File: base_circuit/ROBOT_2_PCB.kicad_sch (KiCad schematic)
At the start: 21 parts, among them J1 Conn_01x04, J2 Output_Supply, J3 Conn_01x01_Female, J4 M1,2, J5 M3,4, M1 Conn_01x04_Female, M2 Conn_01x04_Female, M3 Conn_01x04_Female, M4 Conn_01x04_Female, SW1 SW_SPDT, SW2 SW_SPDT

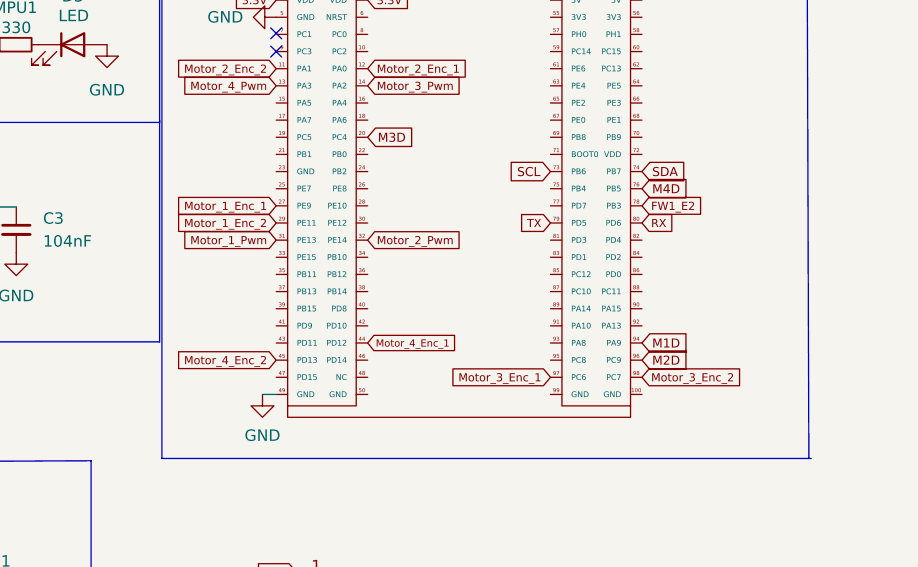
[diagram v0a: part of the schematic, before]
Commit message: Add ioc file od base circuit
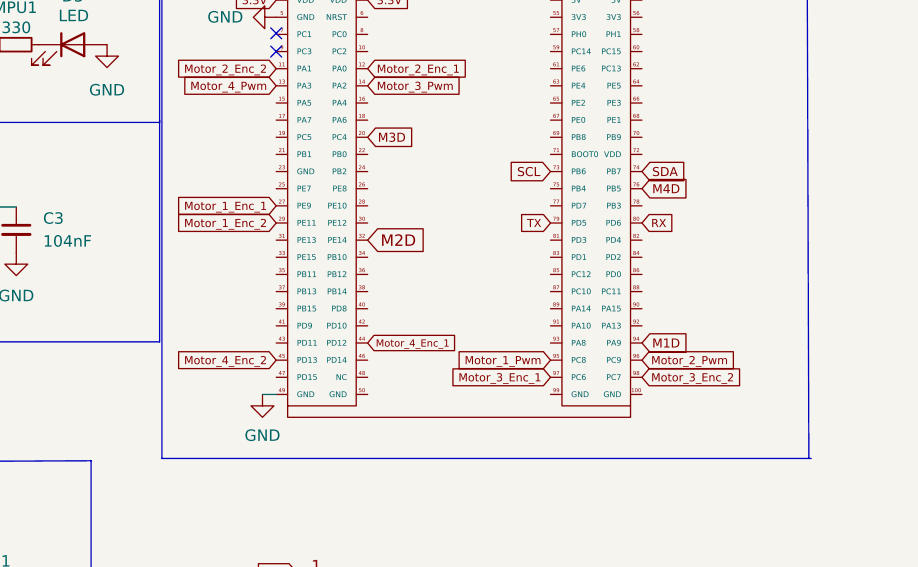
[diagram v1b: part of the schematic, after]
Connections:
- net M2D: now also S1.32 (PE14); no longer S1.96 (PC9)
- net Motor_1_Pwm: now also S1.95 (PC8); no longer S1.31 (PE13)
- net Motor_2_Pwm: now also S1.96 (PC9); no longer S1.32 (PE14)
- net FW1_E2: no longer names the net of S1.78 (PB3)
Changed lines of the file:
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@@
-    )
-  )
-  (global_label "FW1_E2" (shape input) (at 130.048 67.183 0) (fields_autoplaced)
-    (effects (font (size 0.9 0.9)) (justify left))
-    (property "Intersheet References" "${INTERSHEET_REFS}" (id 0) (at 136.7723 67.1268 0)
-      (effects (font (size 0.9 0.9)) (justify left) hide)
     )
   )
@@
     )
   )
+  (global_label "M2D" (shape input) (at 99.568 70.993 0) (fields_autoplaced)
+    (effects (font (size 1.27 1.27)) (justify left))
+    (property "Intersheet References" "${INTERSHEET_REFS}" (id 0) (at 105.9121 70.9136 0)
+      (effects (font (size 1.27 1.27)) (justify left) hide)
+    )
+  )
   (global_label "Motor_2_Enc_2" (shape input) (at 158.496 168.91 180) (fields_autoplaced)
     (effects (font (size 0.9 0.9)) (justify right))
@@
     )
   )
-  (global_label "Motor_1_Pwm" (shape input) (at 89.408 70.993 180) (fields_autoplaced)
-    (effects (font (size 0.9 0.9)) (justify right))
-    (property "Intersheet References" "${INTERSHEET_REFS}" (id 0) (at 78.698 70.9368 0)
+  (global_label "Motor_1_Pwm" (shape input) (at 119.888 84.328 180) (fields_autoplaced)
+    (effects (font (size 0.9 0.9)) (justify right))
+    (property "Intersheet References" "${INTERSHEET_REFS}" (id 0) (at 109.178 84.2718 0)
       (effects (font (size 0.9 0.9)) (justify right) hide)
     )
@@
     (property "Intersheet References" "${INTERSHEET_REFS}" (id 0) (at 107.77 169.8698 0)
       (effects (font (size 0.9 0.9)) (justify right) hide)
-    )
-  )
-  (global_label "M2D" (shape input) (at 130.048 84.328 0) (fields_autoplaced)
-    (effects (font (size 1 1)) (justify left))
-    (property "Intersheet References" "${INTERSHEET_REFS}" (id 0) (at 135.0432 84.2655 0)
-      (effects (font (size 1 1)) (justify left) hide)
     )
   )
@@
     )
   )
-  (global_label "Motor_2_Pwm" (shape input) (at 99.568 70.993 0) (fields_autoplaced)
-    (effects (font (size 0.9 0.9)) (justify left))
-    (property "Intersheet References" "${INTERSHEET_REFS}" (id 0) (at 110.278 70.9368 0)
-      (effects (font (size 0.9 0.9)) (justify left) hide)
-    )
+  (global_label "Motor_2_Pwm" (shape input) (at 130.048 84.328 0) (fields_autoplaced)
+    (effects (font (size 0.9 0.9)) (justify left))
+    (property "Intersheet References" "${INTERSHEET_REFS}" (id 0) (at 140.758 84.2718 0)
+      (effects (font (size 0.9 0.9)) (justify left) hide)
+    )

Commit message: debugging push for singlefile change
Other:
- note added: "laaa****mmmooooo"
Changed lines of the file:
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@@
     (stroke (width 0) (type default) (color 0 0 0 0))
+  )
+  (text "laaa****mmmooooo" (at 22.606 -12.7 0)
+    (effects (font (size 10 10)) (justify left bottom))
   )
   (text "MAIN CONTROLLER BOARD\n" (at 79.248 20.574 0)

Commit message: Final Edit of base circuit
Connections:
- net GND: now also S1.50 (GND)
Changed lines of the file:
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@@
     (pin "4")
+  )
+  (symbol (lib_id "power:GND") (at 99.568 88.138 0) (unit 1)
+    (in_bom yes) (on_board yes) (fields_autoplaced)
+    (property "Reference" "#PWR0112" (id 0) (at 99.568 94.488 0)
+      (effects (font (size 1.27 1.27)) hide)
+    )
+    (property "Value" "GND" (id 1) (at 99.568 92.71 0))
+    (property "Footprint" "" (id 2) (at 99.568 88.138 0)
+      (effects (font (size 1.27 1.27)) hide)
+    )
+    (property "Datasheet" "" (id 3) (at 99.568 88.138 0)
+      (effects (font (size 1.27 1.27)) hide)
+    )
+    (pin "1")
   )
   (symbol (lib_id "Connector_Generic:Conn_01x05") (at 32.004 33.02 0) (unit 1)
@@
       (reference "#PWR0111") (unit 1) (value "GND") (footprint "")
     )
+    (path "/21177c56-f2a5-4c39-9fca-9dfafd9b0072"
+      (reference "#PWR0112") (unit 1) (value "GND") (footprint "")
+    )
     (path "/86c17262-2c7a-4ee7-bb6b-b97ffef60f30"

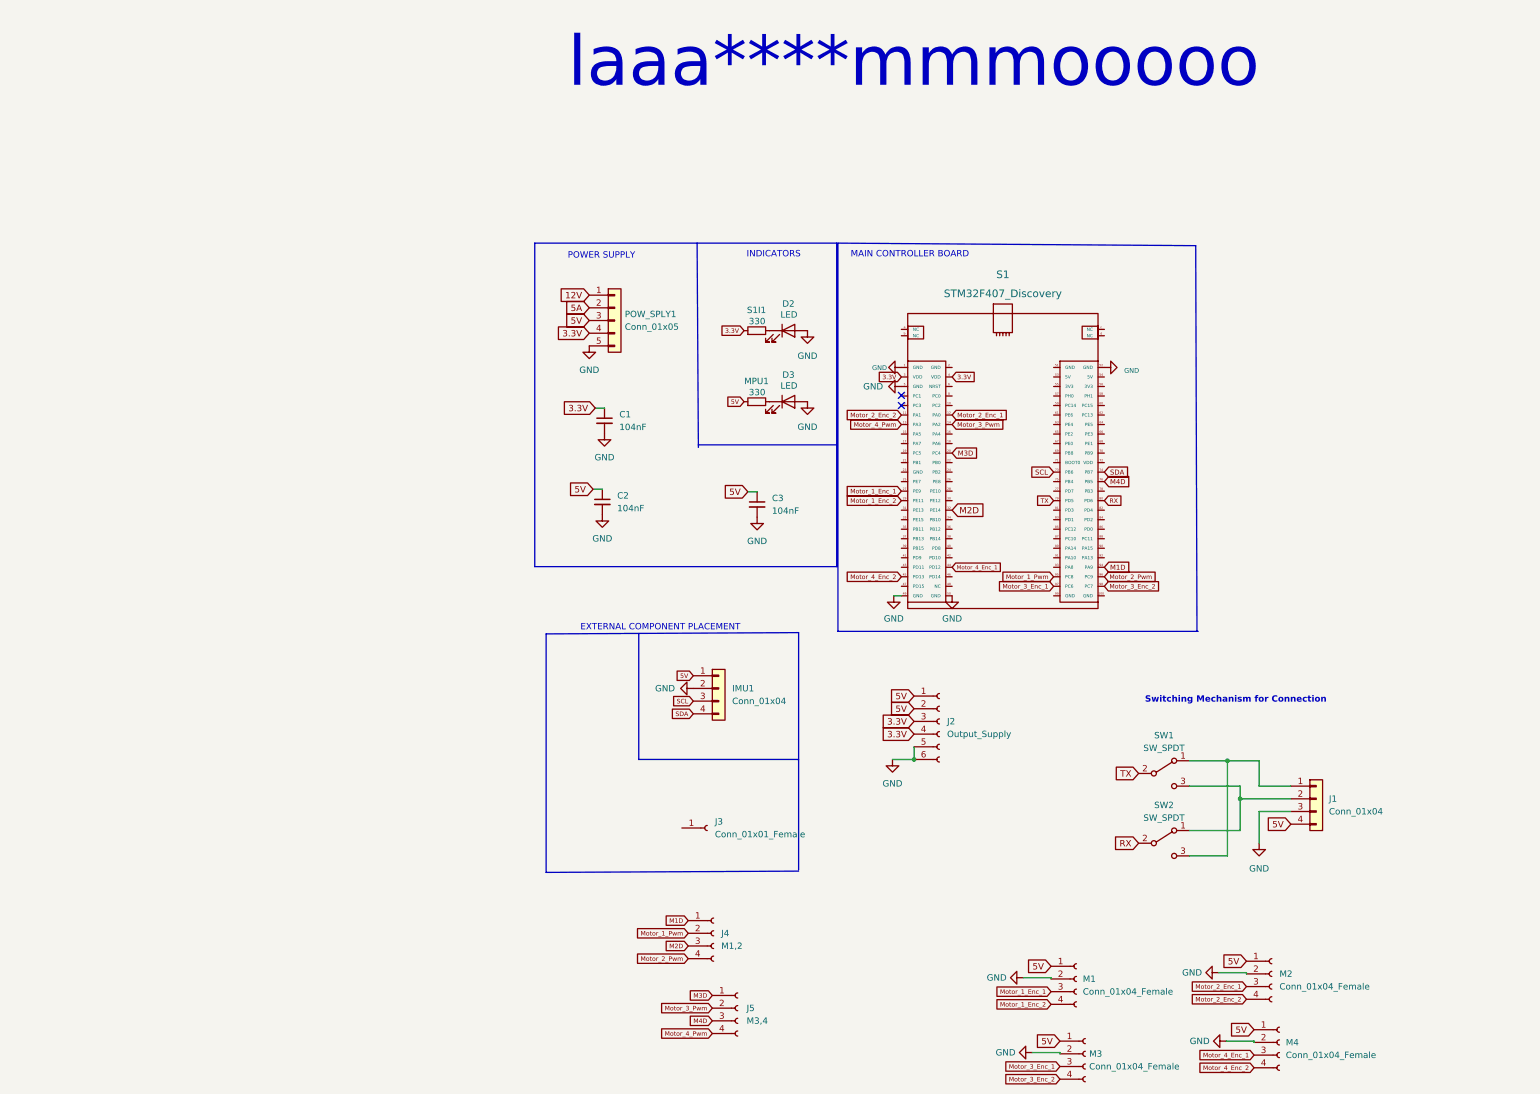
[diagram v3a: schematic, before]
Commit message: Add mounting holes and clean schematic
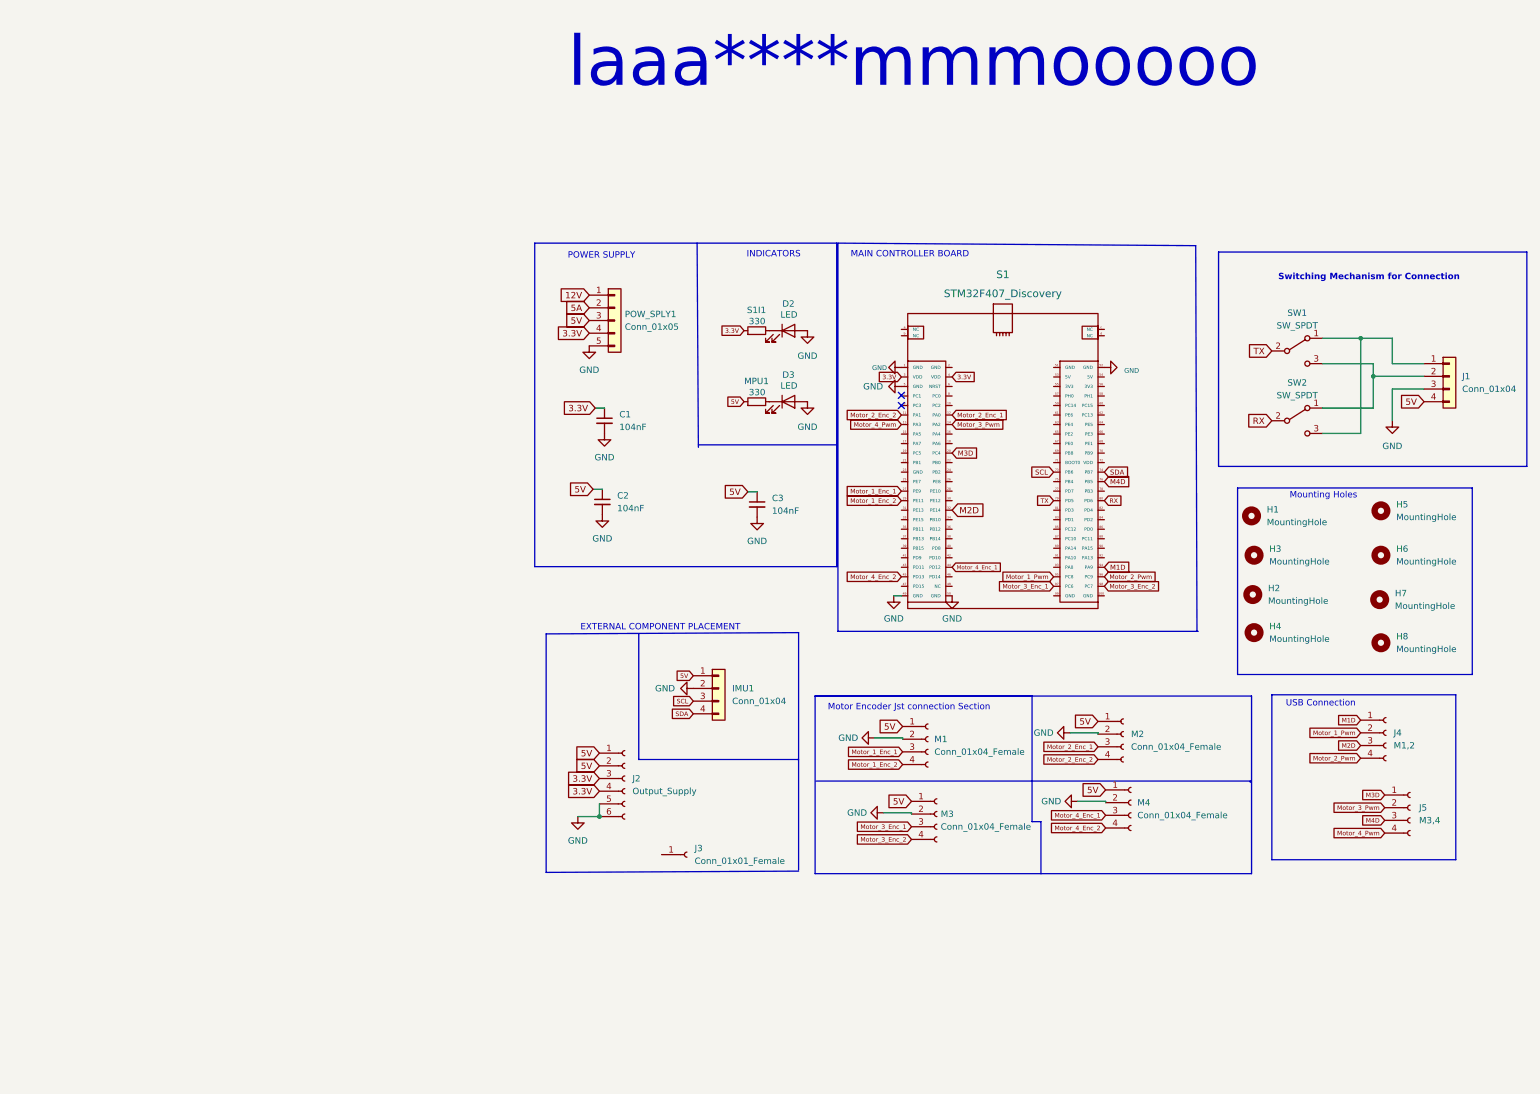
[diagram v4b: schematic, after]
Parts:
- added H1, H2, H3, H4, H5, H6, H7, H8: MountingHole, MountingHole:MountingHole_3mm, symbol Mechanical:MountingHole
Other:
- note added: "Motor Encoder Jst connection Section"
- note added: "Mounting Holes"
- note added: "USB Connection"
- moved on the sheet: J1, J2, J3, J4, J5, M1, M2, M3, M4, SW1, SW2

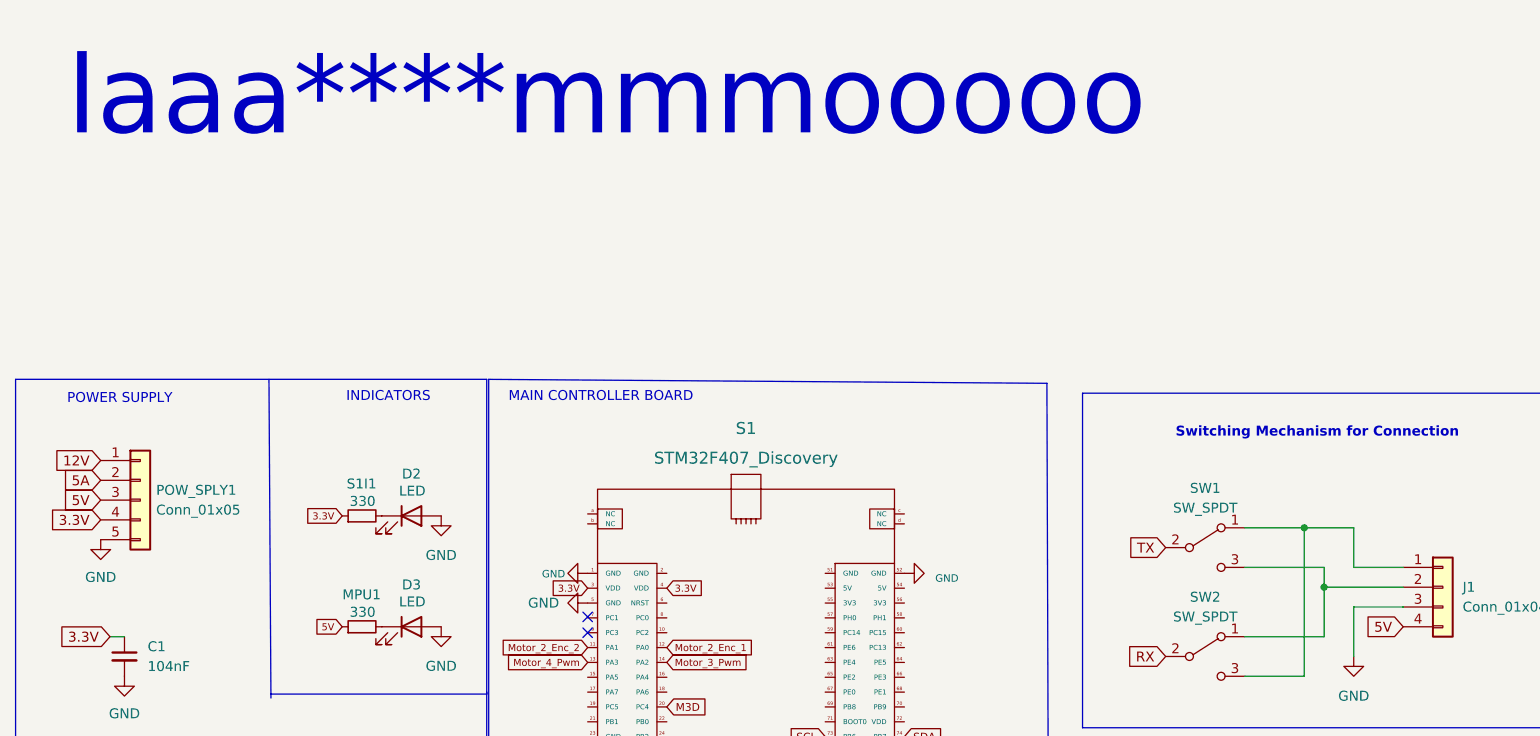
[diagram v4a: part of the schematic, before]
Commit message: Edit Orientation and References and ready for printing
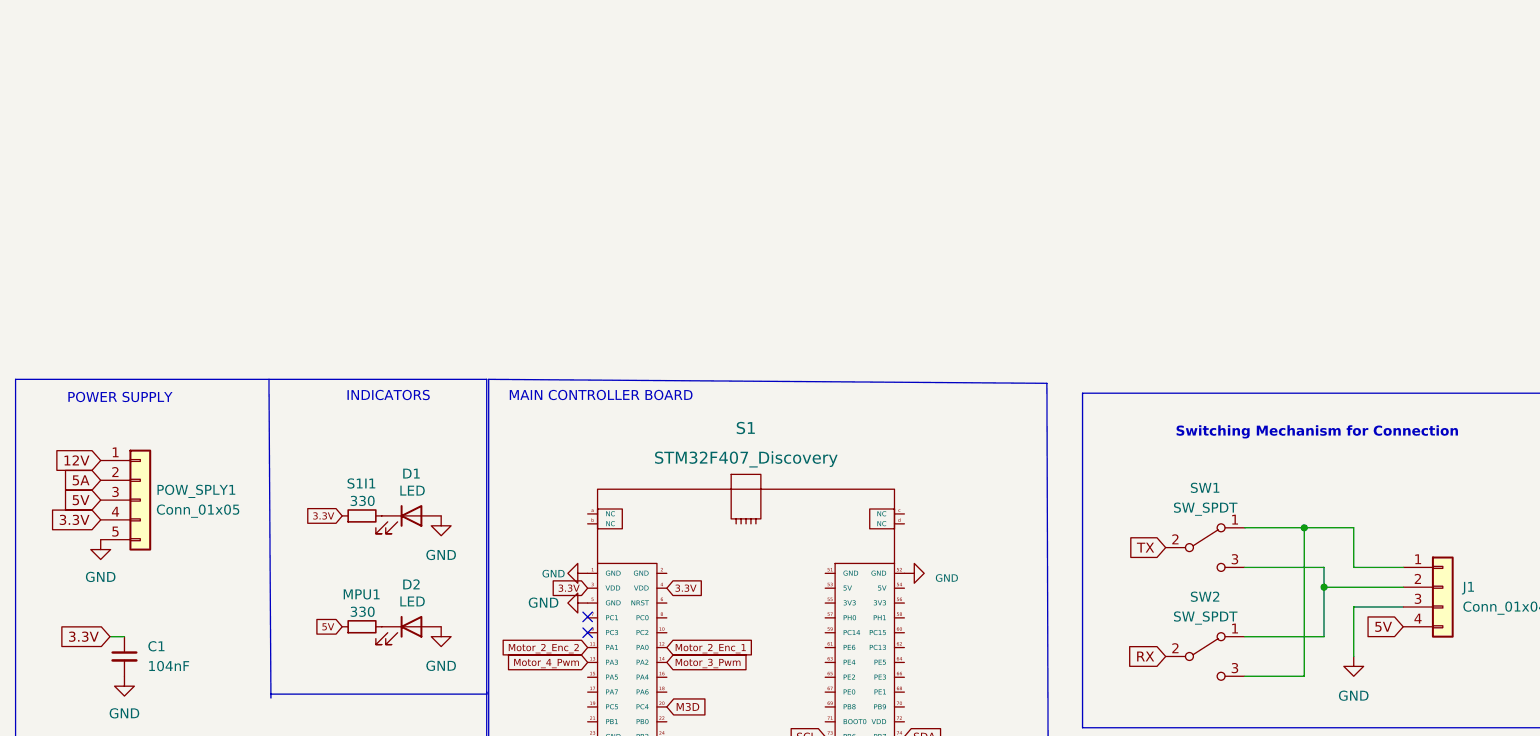
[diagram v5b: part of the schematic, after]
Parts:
- renumbered D2 to D1, D3 to D2
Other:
- note removed: "laaa****mmmooooo"
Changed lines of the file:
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@@
     (stroke (width 0) (type default) (color 0 0 0 0))
-  )
-  (text "laaa****mmmooooo" (at 22.606 -12.7 0)
-    (effects (font (size 10 10)) (justify left bottom))
   )
   (text "MAIN CONTROLLER BOARD\n" (at 79.248 20.574 0)
@@
   (symbol (lib_id "Device:LED") (at 66.802 49.276 0) (unit 1)
     (in_bom yes) (on_board yes)
-    (property "Reference" "D3" (id 0) (at 66.802 43.8912 0))
+    (property "Reference" "D2" (id 0) (at 66.802 43.8912 0))
     (property "Value" "LED" (id 1) (at 66.9036 46.0756 0))
     (property "Footprint" "modfiles:LED_D3.0mm" (id 2) (at 66.802 49.276 0)
@@
   (symbol (lib_id "Device:LED") (at 66.802 35.052 0) (unit 1)
     (in_bom yes) (on_board yes)
-    (property "Reference" "D2" (id 0) (at 66.802 29.6672 0))
+    (property "Reference" "D1" (id 0) (at 66.802 29.6672 0))
     (property "Value" "LED" (id 1) (at 66.9036 31.8516 0))
     (property "Footprint" "modfiles:LED_D3.0mm" (id 2) (at 66.802 35.052 0)
@@
     )
     (path "/ac9fbfc9-01d9-4859-b7bb-c68e84be9007"
+      (reference "D1") (unit 1) (value "LED") (footprint "modfiles:LED_D3.0mm")
+    )
+    (path "/6ec4df7d-5b0a-4839-b8fa-e2e30756b36d"
       (reference "D2") (unit 1) (value "LED") (footprint "modfiles:LED_D3.0mm")
     )
-    (path "/6ec4df7d-5b0a-4839-b8fa-e2e30756b36d"
-      (reference "D3") (unit 1) (value "LED") (footprint "modfiles:LED_D3.0mm")
-    )
     (path "/7b79e480-afa8-4a28-b14b-e86c879b6938"

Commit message: Kam vairaxa
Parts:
- removed D1: LED, modfiles:LED_D3.0mm, symbol Device:LED
- removed J2: Output_Supply, modfiles:JST_5_BIG, symbol Connector:Conn_01x06_Female
- removed S1I1: 330, modfiles:Resistor_small, symbol Device:R_Small
- added C4, C5: C_Small, modfiles:Capacitor_Disc_Small, symbol Device:C_Small
- added D1, D3, D4, D5, D6, D7: LED_Small, modfiles:LED_D3.0mm, symbol Device:LED_Small
- added F1: Fuse_Small, modfiles:Fuse_Holder, symbol Device:Fuse_Small
- added J2, J6, J7: Conn_01x02_Male, modfiles:Connector_Bornier_2, symbol Connector:Conn_01x02_Male
- added R1, R2, R3, R4, R5, R6: R_Small, modfiles:Resistor_small, symbol Device:R_Small
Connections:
- net 12V: now also D4.2 (A)
- net 3.3V: now also D5.2 (A), F1.1; no longer C1.1, S1.3 (VDD), S1.4 (VDD)
- net 5A: now also D3.2 (A)
- net 5V: now also C4.1, D6.2 (A), D7.2 (A), J2.1 (Pin_1), J2.2 (Pin_2)
- net GND: now also D2.1 (K), S1.100 (GND), S1.2 (GND), S1.23 (GND), S1.51 (GND), S1.99 (GND), C4.2, C5.2, J7.1 (Pin_1), J7.2 (Pin_2), R1.2, R2.2, R3.2, R4.2, R5.1, R6.2; no longer D2.2 (A)
- net Motor_1_Enc_1: now also S1.12 (PA0); no longer S1.27 (PE9)
- net Motor_1_Enc_2: now also S1.11 (PA1); no longer S1.29 (PE11)
- net Motor_2_Enc_1: now also S1.27 (PE9); no longer S1.12 (PA0)
- net Motor_2_Enc_2: now also S1.29 (PE11); no longer S1.11 (PA1)
- net Motor_3_Enc_1: now also S1.44 (PD12); no longer S1.97 (PC6)
- net Motor_3_Enc_2: now also S1.45 (PD13); no longer S1.98 (PC7)
- net Motor_4_Enc_1: now also S1.97 (PC6); no longer S1.44 (PD12)
- net Motor_4_Enc_2: now also S1.98 (PC7); no longer S1.45 (PD13)
- net at MPU1.2: now also D2.2 (A); no longer D2.1 (K)
- new net: D1.1 (K), R6.1
- new net: D5.1 (K), R3.1
- new net: D4.1 (K), R2.1
- new net: D7.1 (K), R5.2
- new net: D6.1 (K), R4.1
- new net: D3.1 (K), R1.1
- new net 3V3: C5.1, J6.1 (Pin_1), J6.2 (Pin_2)
- new net VDD: C1.1, D1.2 (A), F1.2, S1.3 (VDD), S1.4 (VDD)
- no-connect marks 2 -> 72
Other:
- moved on the sheet: C1, C2, C3, D2, J3
